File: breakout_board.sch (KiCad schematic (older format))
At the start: 19 parts, among them J1 PJ-102A, J2 Conn_01x09_Male, J3 Conn_01x09_Male, J4 Conn_01x10_Male, J5 Conn_01x08_Male, J6 Conn_01x09_Male, J7 Conn_01x10_Male, J8 Conn_01x02_Male, J9 AVR-ISP-6, U1 ATmega1281-16AU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

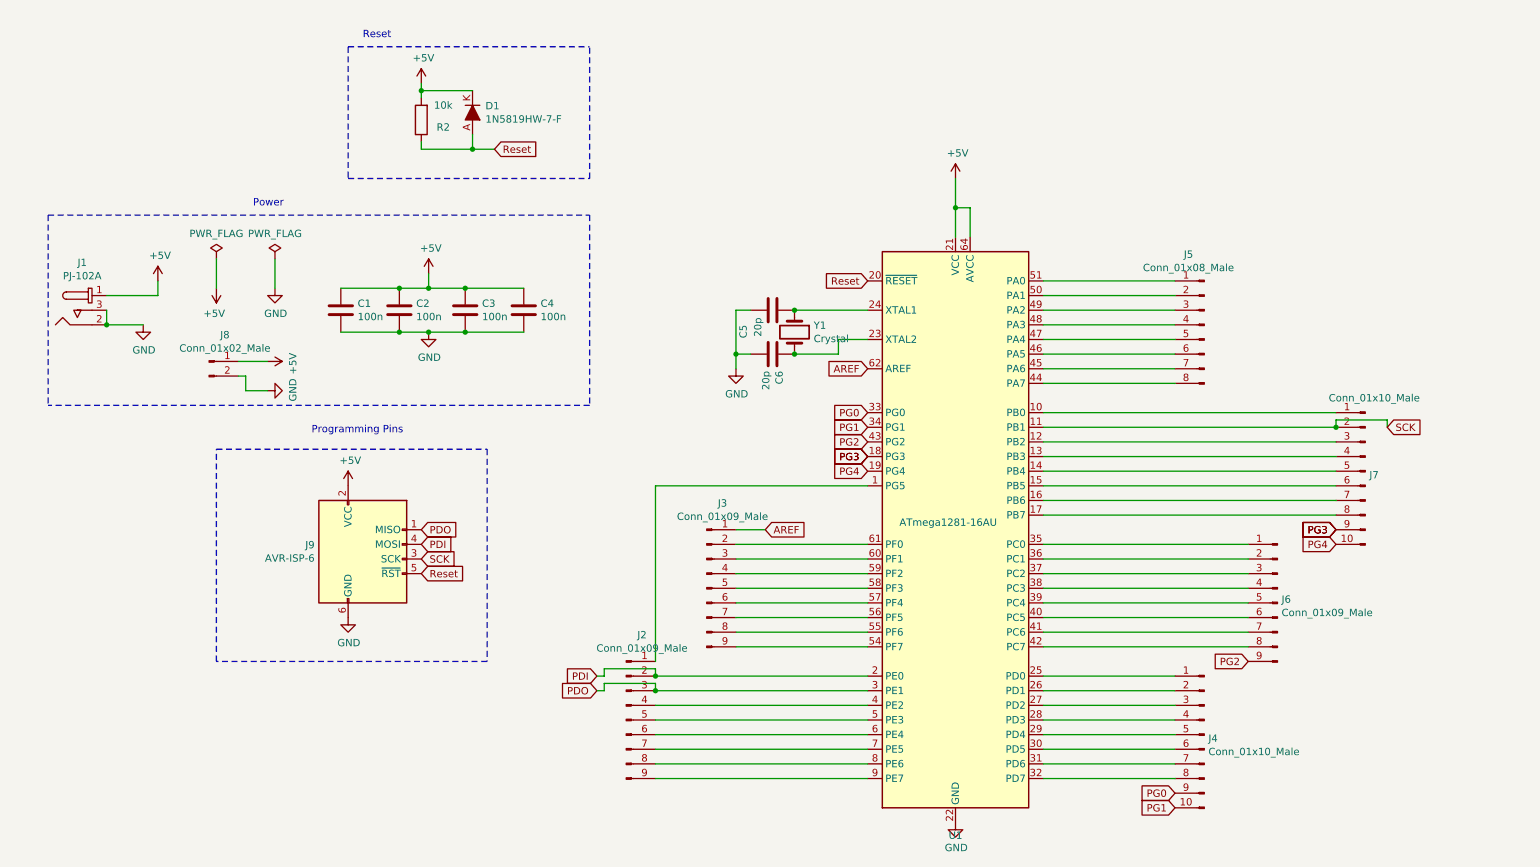
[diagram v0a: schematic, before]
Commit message: Add files via upload
Fixed incorrect silkscreen pin labels, added silkscreen labels for pin functionality. Added reset button to reset the microcontroller
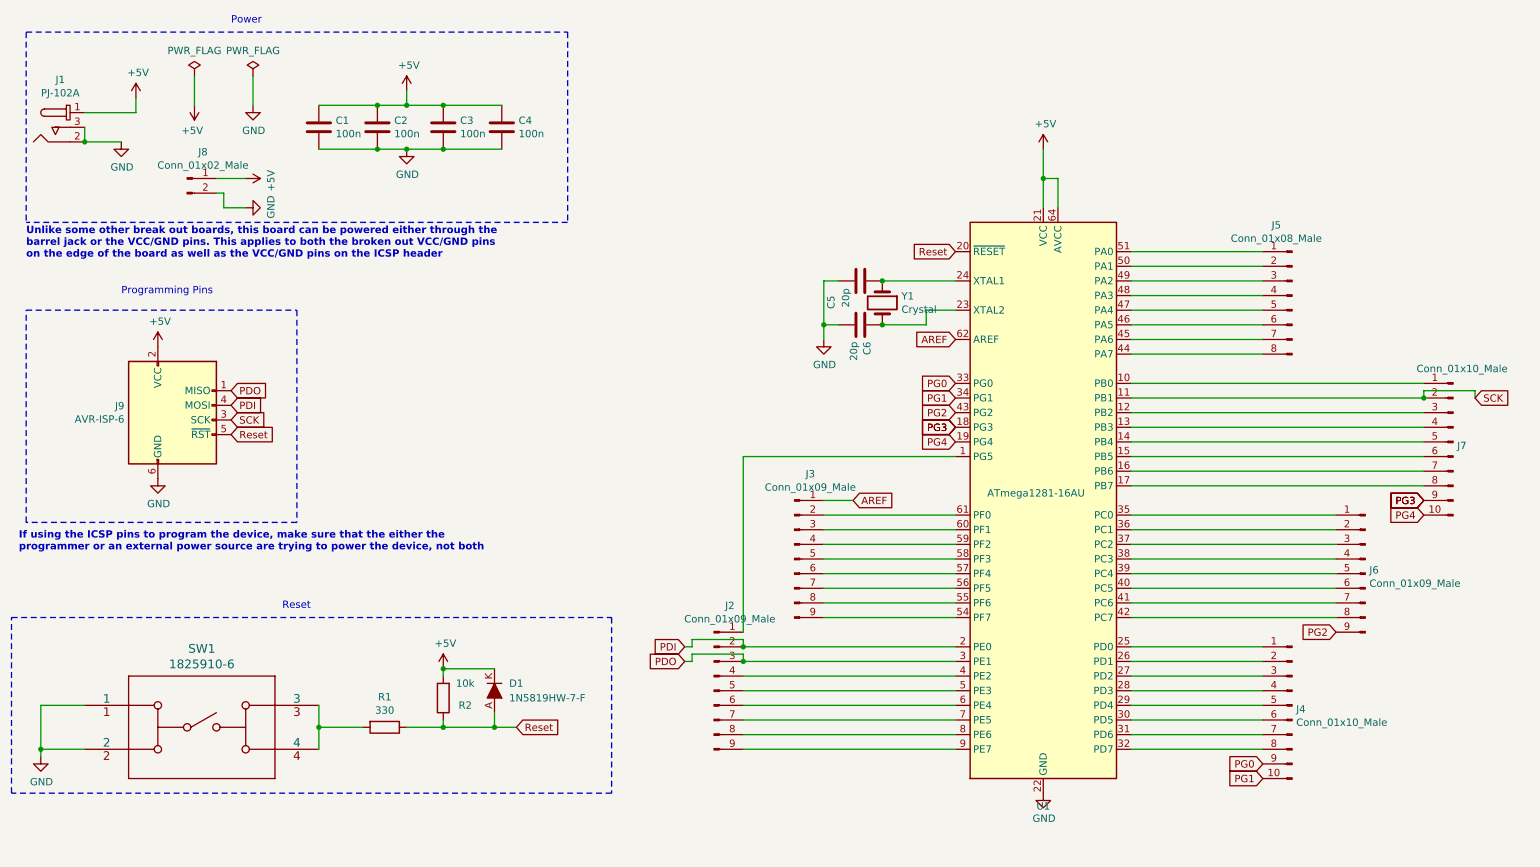
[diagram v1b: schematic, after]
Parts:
- added R1: 330, Resistor_SMD:R_0805_2012Metric_Pad1.15x1.40mm_HandSolder, symbol Device:R
- added SW1: 1825910-6, footprints:1825910-6, symbol 2020-08-10_02-55-49:1825910-6
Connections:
- net GND: now also SW1.1, SW1.2
- net Reset: now also R1.1
- new net: R1.2, SW1.3, SW1.4
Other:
- note added: "If using the ICSP pins to program the device, make sure that the either the\nprogrammer or an external power source are trying to power the device, not both"
- note added: "Reset"
- note added: "Unlike some other break out boards, this board can be powered either through the \nbarrel jack or the VCC/GND pins. This applies to both the broken out VCC/GND pins \non the edge of the board as well as the VCC/GND pins on the ICSP header"
- note removed: "Reset\n"
- moved on the sheet: C1, C2, C3, C4, C5, C6, D1, J1, J2, J3, J4, J5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
